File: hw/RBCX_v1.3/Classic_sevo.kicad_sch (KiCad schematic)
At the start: 14 parts

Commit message: Work in progress
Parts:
- D15: renamed from D?; footprint Package_TO_SOT_SMD:SOT-23 -> Package_TO_SOT_SMD:SOT-523; LCSC C2828465 -> C134414
- gave numbers to parts that had none: 13
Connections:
- net 3V3: now also U14.3 (VCC); no longer U14.5 (VCC)
- net at R110.1: now also U14.6 (OUT); no longer U14.1 (REF)
- net SERVO1_PWR renamed SERVO_PWR
- net SERVO_PWR: now also U14.4 (IN+); no longer U14.3 (IN+)
- net SERVO_1 renamed SERVO
- net SERVO_1_PWR renamed SERVO-PWR
- net SERVO-PWR: now also U14.5 (IN-); no longer U14.4 (IN-)

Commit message: New PCB layout
some changes of schema:
- change PD sink AO33772 to AO33771
- remove power switch
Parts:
- J37: footprint Connector_PinHeader_2.54mm:PinHeader_1x03_P2.54mm_Vertical -> RBCX:PinHeader_1x03_P2.54mm_Vertical
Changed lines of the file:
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@@
       (effects (font (size 1.27 1.27)) (justify left))
     )
-    (property "Footprint" "Connector_PinHeader_2.54mm:PinHeader_1x03_P2.54mm_Vertical" (id 2) (at 135.89 83.82 0)
+    (property "Footprint" "RBCX:PinHeader_1x03_P2.54mm_Vertical" (id 2) (at 135.89 83.82 0)
       (effects (font (size 1.27 1.27)) hide)
     )

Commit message: Production files
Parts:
- D15, U14: JLCPCB_CORRECTION (none) -> 0;0;180
- J37: JLCPCB_CORRECTION (none) -> 0;-2.54;90
- TP38, TP39, TP40: JLCPCB_IGNORE (none) -> 1
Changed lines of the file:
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@@
+      (effects (font (size 1.27 1.27)) hide)
+    )
+    (property "JLCPCB_IGNORE" "1" (id 4) (at 83.82 78.74 0)
       (effects (font (size 1.27 1.27)) hide)
     )
@@
       (effects (font (size 1.27 1.27)) hide)
     )
+    (property "JLCPCB_IGNORE" "1" (id 4) (at 114.3 67.437 0)
+      (effects (font (size 1.27 1.27)) hide)
+    )
     (pin "P$1")
   )
@@
       (effects (font (size 1.27 1.27)) hide)
     )
+    (property "JLCPCB_CORRECTION" "0;0;180" (id 6) (at 93.98 81.28 0)
+      (effects (font (size 1.27 1.27)) hide)
+    )
     (pin "1")
     (pin "2")
@@
       (effects (font (size 1.27 1.27)) hide)
     )
+    (property "JLCPCB_CORRECTION" "0;-2.54;90" (id 6) (at 135.89 83.82 0)
+      (effects (font (size 1.27 1.27)) hide)
+    )
     (pin "1")
     (pin "2")
@@
       (effects (font (size 1.27 1.27)) hide)
     )
+    (property "JLCPCB_IGNORE" "1" (id 4) (at 78.74 48.387 0)
+      (effects (font (size 1.27 1.27)) hide)
+    )
     (pin "P$1")
   )
@@
       (effects (font (size 1.27 1.27)) hide)
     )
+    (property "JLCPCB_CORRECTION" "0;0;180" (id 6) (at 102.87 50.927 0)
+      (effects (font (size 1.27 1.27)) hide)
+    )

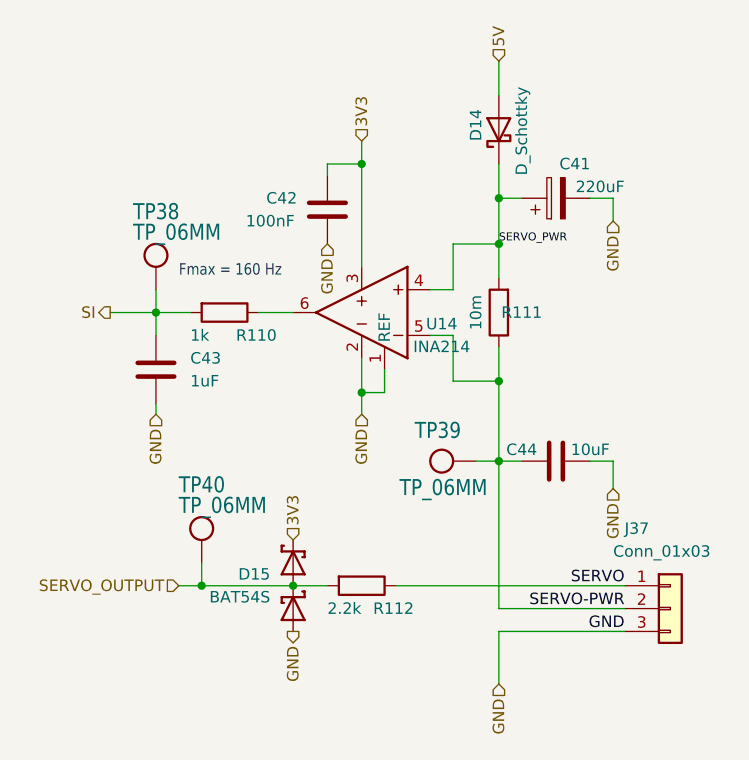
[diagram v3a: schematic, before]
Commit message: Kuba issues
Change of power transistor from JSM3622 to JMSL0302AU

NTC connectors

Moving the Cell balancer behind the switch

and some little things
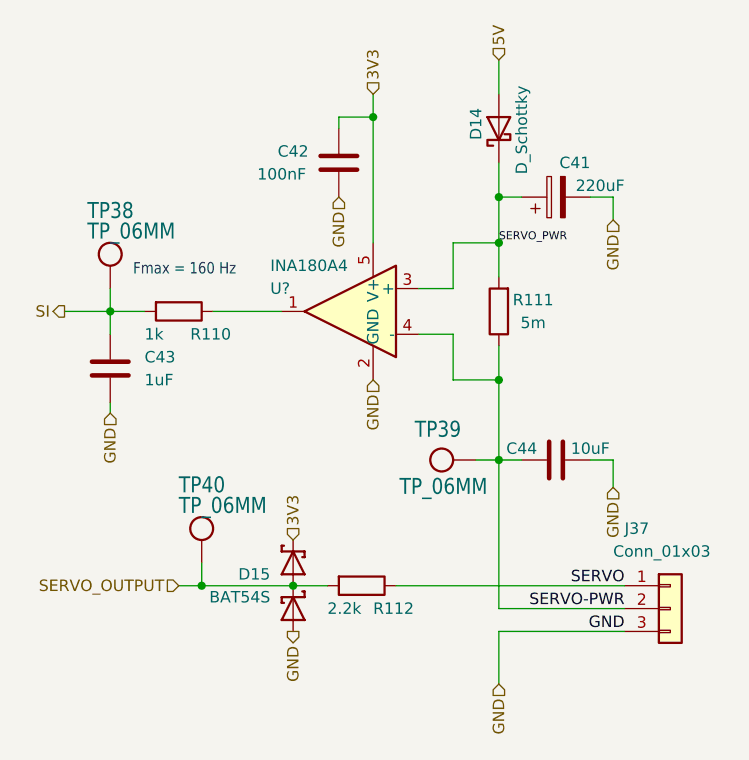
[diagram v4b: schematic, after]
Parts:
- removed U14: INA214, Package_TO_SOT_SMD:SOT-363_SC-70-6, symbol RBCX:INA214
- added U?: INA180A4, Package_TO_SOT_SMD:SOT-23-5, symbol Amplifier_Current:INA180A4
- R111: value 10m -> 5m; LCSC C728271 -> C728267
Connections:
- net 3V3: now also U?.5 (V+)
- net GND: now also U?.2 (GND)
- net SERVO-PWR: now also U?.4 (-)
- net SERVO_PWR: now also U?.3 (+)
- net at R110.1: now also U?.1
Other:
- moved on the sheet: C42, C43, R110, TP38

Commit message: Kuba issues - PCB
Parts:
- gave numbers to parts that had none: 1
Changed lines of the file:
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@@
   (symbol (lib_id "Amplifier_Current:INA180A4") (at 100.33 50.8 0) (mirror y) (unit 1)
     (in_bom yes) (on_board yes)
-    (property "Reference" "U?" (id 0) (at 91.44 48.26 0)
+    (property "Reference" "U14" (id 0) (at 91.44 48.26 0)
       (effects (font (size 1.27 1.27)) (justify right))
     )
